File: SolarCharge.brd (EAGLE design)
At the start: 63 x 63 mm, 9 parts

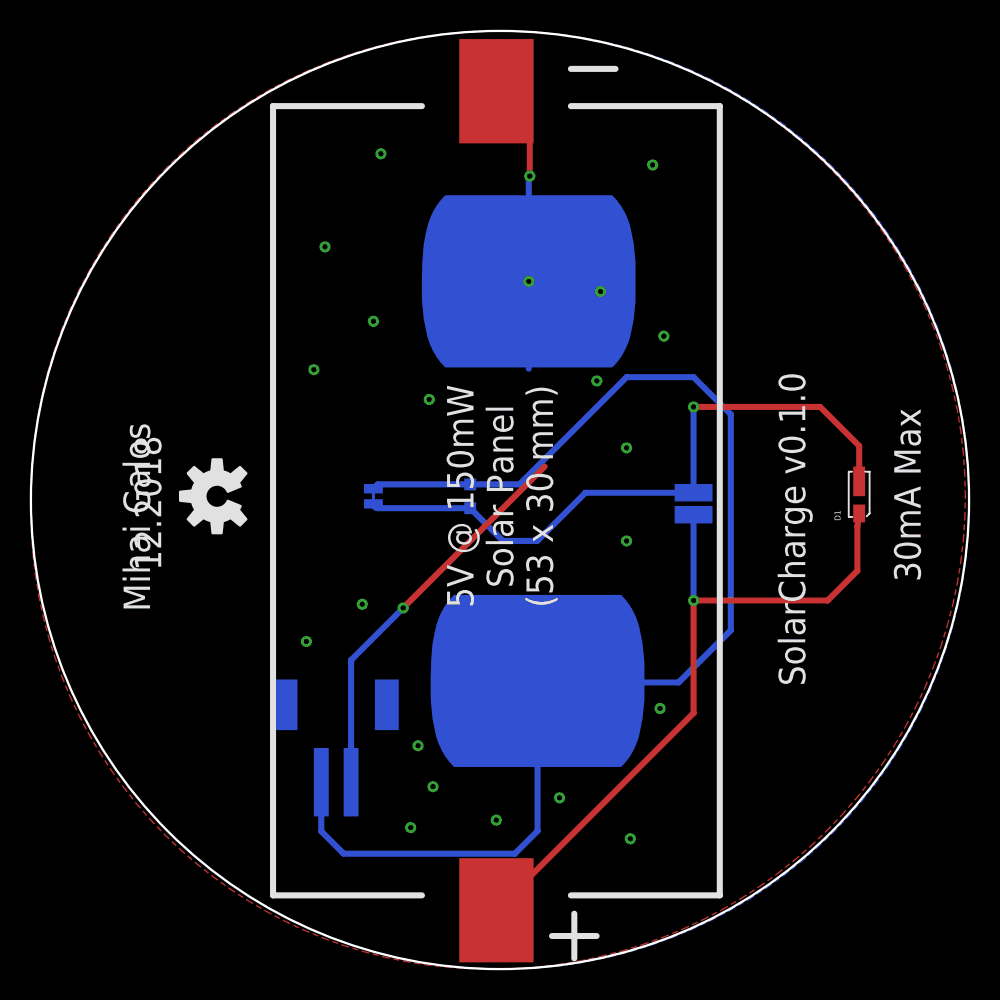
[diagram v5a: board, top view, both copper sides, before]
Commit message: Add RGB runtime info
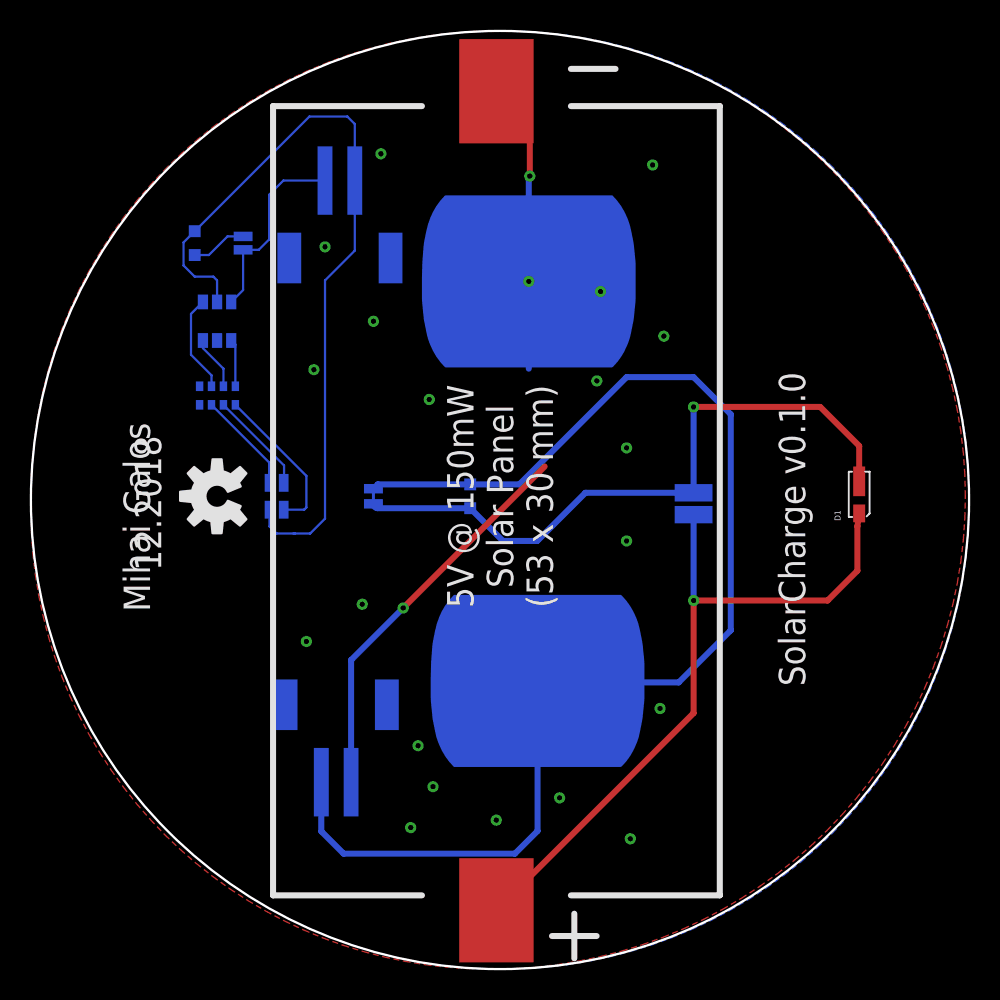
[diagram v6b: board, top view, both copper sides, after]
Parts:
- added CN2: (no value), lio:JST-PH-2-SMT-RA
- added LED1: GM1WA55311A, led:GM1WA55311A
- added R2: (no value), ROHM:0603-RES
- added R3: 470Ω, SparkFun:0603-ARV
- added SJ2: SOLDERJUMPERNO, SparkFun-Passives:SJ_2S-NO
- added U1: TINY4/5/9/10-TSHR/TS8R, bt_avr:SOT-23-6
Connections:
- new net +3V3: CN2.1, LED1.4, R2.1, U1.5
- new net BLUE: R3.3, U1.3
- new net GREEN: R3.2, U1.4
- new net N$5: LED1.3, R3.6
- new net N$6: LED1.2, R3.7
- new net N$7: R2.2, SJ2.2
- new net RED: R3.4, U1.1
- new net RED_RESISTOR: LED1.1, R3.5
- new net RXD: CN2.2, SJ2.1, U1.6
- net GND: now also U1.2
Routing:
- net +3V3: track 0.00 -> 54.0 mm
- net RXD: track 0.00 -> 13.3 mm
- net RED_RESISTOR: track 0.00 -> 10.6 mm
- net N$5: track 0.00 -> 7.04 mm
- net N$6: track 0.00 -> 6.89 mm
- net GREEN: track 0.00 -> 6.81 mm
- net N$7: track 0.00 -> 3.77 mm
- net BLUE: track 0.00 -> 3.64 mm
- net RED: track 0.00 -> 3.58 mm
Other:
- board text removed: "30mA Max"

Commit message: Add second JST connector for solar out
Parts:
- added CN3: (no value), lio:JST-PH-2-SMT-RA
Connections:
- net GND: now also CN3.2
- net N$4: now also CN3.1
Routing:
- net N$4: track 86.3 -> 96.7 mm
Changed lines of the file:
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@@
 <element name="CN2" library="lio" package="JST-PH-2-SMT-RA" value="" x="9.75" y="49" rot="MR180"/>
 <element name="SJ2" library="SparkFun-Passives" package="SJ_2S-NO" value="SOLDERJUMPERNO" x="3.25" y="48.5" rot="MR90"/>
+<element name="CN3" library="lio" package="JST-PH-2-SMT-RA" value="" x="37.5" y="16" rot="MR0"/>
 </elements>
 <signals>
@@
 <via x="15" y="14.75" extent="1-16" drill="0.35"/>
 <contactref element="U1" pad="2"/>
+<contactref element="CN3" pad="2"/>
+<wire x1="22.5" y1="53" x2="30.75" y2="53.75" width="0" layer="19" extent="1-1"/>
+<wire x1="27" y1="39.25" x2="22.432" y2="40.068" width="0" layer="19" extent="16-16"/>
+<wire x1="27.25" y1="45.25" x2="22.432" y2="45.93" width="0" layer="19" extent="16-16"/>
+<wire x1="29" y1="34.75" x2="27" y2="39.25" width="0" layer="19" extent="1-1"/>
+<wire x1="31.5" y1="42.25" x2="27.25" y2="45.25" width="0" layer="19" extent="1-1"/>
+<wire x1="23.5" y1="33.5" x2="29" y2="34.75" width="0" layer="19" extent="1-1"/>
+<wire x1="11.25" y1="24.25" x2="14" y2="24" width="0" layer="19" extent="1-1"/>
+<wire x1="7.5" y1="21.75" x2="10.5" y2="20.5" width="0" layer="19" extent="16-16"/>
+<wire x1="14.5" y1="9.25" x2="10.5" y2="12.3" width="0" layer="19" extent="16-16"/>
+<wire x1="16" y1="12" x2="14.5" y2="9.25" width="0" layer="19" extent="1-1"/>
+<wire x1="15" y1="14.75" x2="16" y2="12" width="0" layer="19" extent="1-1"/>
+<wire x1="20.25" y1="9.75" x2="16" y2="12" width="0" layer="19" extent="1-1"/>
+<wire x1="24.5" y1="11.25" x2="20.25" y2="9.75" width="0" layer="19" extent="1-1"/>
+<wire x1="29.25" y1="8.5" x2="24.5" y2="11.25" width="0" layer="19" extent="1-1"/>
+<wire x1="29" y1="28.5" x2="29" y2="34.75" width="0" layer="19" extent="1-1"/>
+<wire x1="15.75" y1="38" x2="22.432" y2="40.068" width="0" layer="19" extent="16-16"/>
+<wire x1="12" y1="43.25" x2="15.75" y2="38" width="0" layer="19" extent="1-1"/>
+<wire x1="8" y1="40" x2="12" y2="43.25" width="0" layer="19" extent="1-1"/>
+<wire x1="8.75" y1="48.25" x2="12" y2="43.25" width="0" layer="19" extent="1-1"/>
+<wire x1="1.5" y1="41.96" x2="8" y2="40" width="0" layer="19" extent="16-16"/>
+<wire x1="12.5" y1="54.5" x2="8.75" y2="48.25" width="0" layer="19" extent="1-1"/>
+<wire x1="31.25" y1="17.25" x2="29.25" y2="8.5" width="0" layer="19" extent="1-1"/>
+<wire x1="38.5" y1="12.3" x2="10.5" y2="12.3" width="0" layer="19" extent="1-16"/>
 </signal>
 <signal name="N$3">
@@
 <wire x1="29" y1="39.5" x2="33.5" y2="39.5" width="0.4064" layer="16"/>
 <wire x1="33.5" y1="39.5" x2="36" y2="37" width="0.4064" layer="16"/>
-<wire x1="36" y1="22.5" x2="32.5" y2="19" width="0.4064" layer="16"/>
-<wire x1="32.5" y1="19" x2="23.122" y2="19" width="0.4064" layer="16"/>
 <wire x1="23.122" y1="19" x2="23.022" y2="19.1" width="0.4064" layer="16"/>
 <wire x1="21.8" y1="32.3" x2="29" y2="39.5" width="0.4064" layer="16"/>
@@
 <wire x1="21.5" y1="7.5" x2="23.022" y2="9.022" width="0.4064" layer="16"/>
 <wire x1="23.022" y1="9.022" x2="23.022" y2="19.1" width="0.4064" layer="16"/>
+<contactref element="CN3" pad="1"/>
+<wire x1="36" y1="22.5" x2="35.75" y2="22.25" width="0.4064" layer="16"/>
+<wire x1="26.172" y1="22.25" x2="23.022" y2="19.1" width="0.4064" layer="16"/>
+<wire x1="35.75" y1="22.25" x2="26.172" y2="22.25" width="0.4064" layer="16"/>
+<wire x1="36.5" y1="12.3" x2="36.5" y2="22" width="0.4064" layer="16"/>
+<wire x1="36.5" y1="22" x2="36" y2="22.5" width="0.4064" layer="16"/>
 </signal>
 <signal name="RXD">

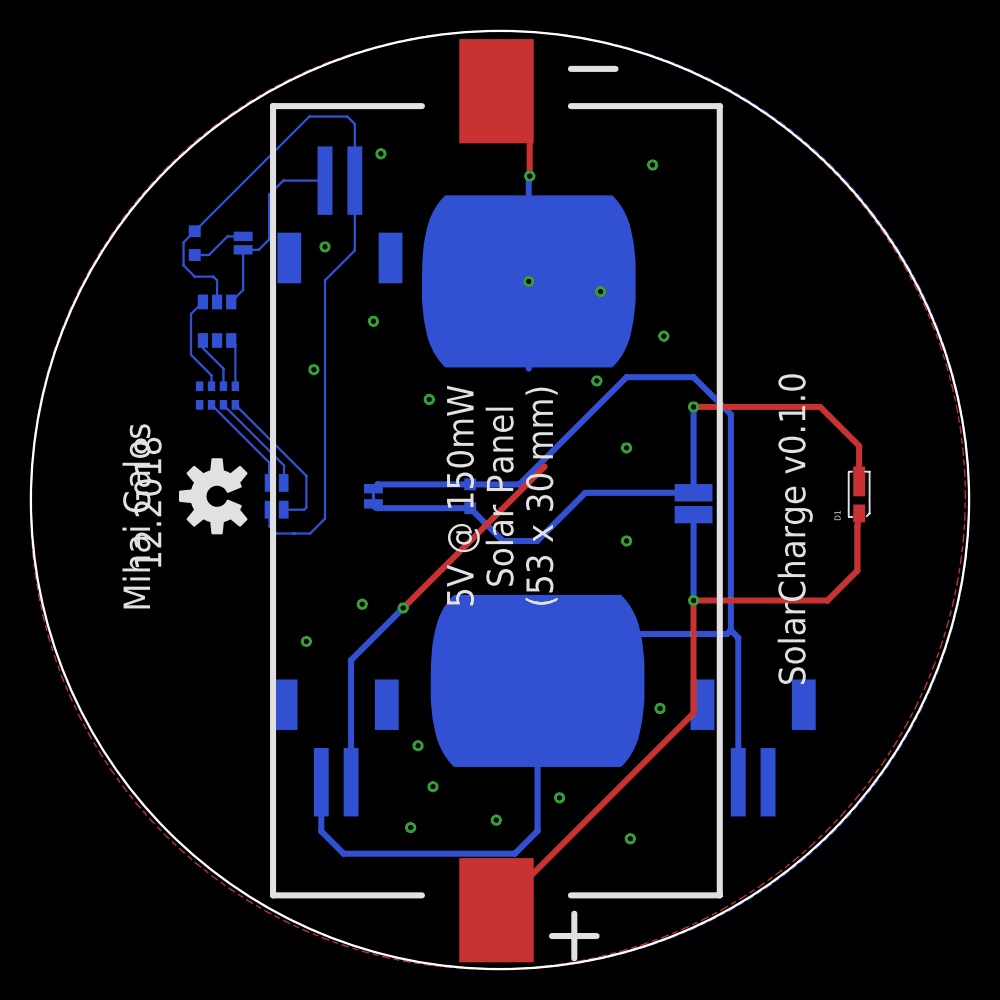
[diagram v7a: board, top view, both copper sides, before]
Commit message: Add Boost coverter to hookup Pi Zero W
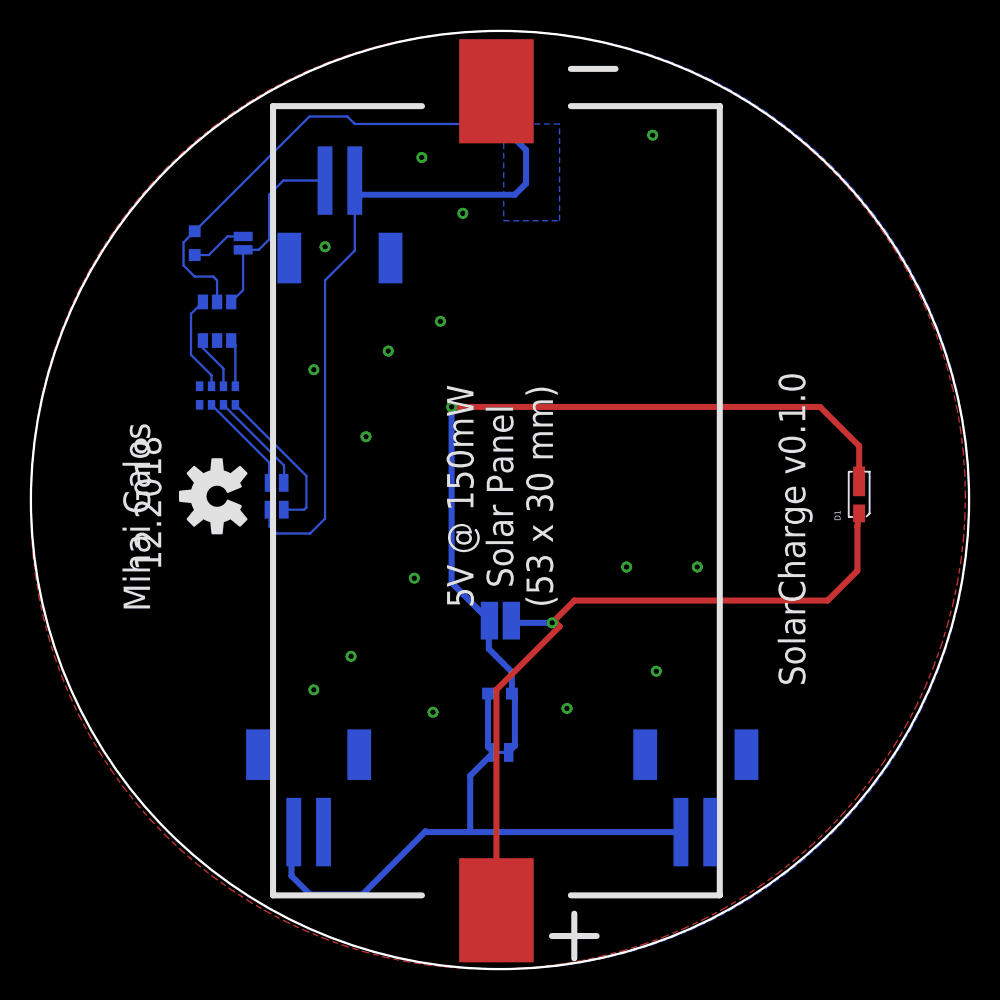
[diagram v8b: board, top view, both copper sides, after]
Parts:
- removed J1, J2: (no value), SparkFun-Connectors:STARBOARD_GROUND_WIDE
- moved SJ1 19.2 mm to (20.6, 14.3), turned to 0 degrees
- moved J3 15.2 mm to (20.5, 23.1), turned to 0 degrees
- moved R1 13.4 mm to (20.5, 18.2), turned to 0 degrees
- moved CN3 5.10 mm to (33.6, 12.7)
- moved CN1 3.83 mm to (7.65, 12.7)
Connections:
- net GND: no longer J2.GROUND
- net N$4: no longer J1.GROUND
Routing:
- net N$4: track 96.7 -> 41.6 mm
- net GND: track 46.2 -> 3.17 mm, vias 23 -> 16
- net +3V3: track 54.0 -> 76.1 mm
- net N$3: track 44.2 -> 56.0 mm
- net N$1: track 47.7 -> 50.0 mm
- added copper zone on layer 16, net +3V3
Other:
- board text added: "Boost regulator 17.55 x 25.22"
- board text added: "In"
- board text added: "Out"
